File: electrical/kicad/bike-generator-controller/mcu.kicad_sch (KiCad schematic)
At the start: 0 parts

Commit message: feat: integrate controller modules and schematics
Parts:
- added U2: DFR0868 Beetle ESP32-C3, symbol BikeGenerator:DFR0868_Beetle_ESP32-C3
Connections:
- new net +3V3: U2.2 (3V3)
- new net GND: U2.1 (GND_L), U2.10 (GND_R)
- new net I2C_SCL: U2.4 (GPIO1)
- new net I2C_SDA: U2.3 (GPIO0)
- new net INA_ALERT: U2.16 (GPIO2)
- new net POT_CS: U2.7 (GPIO5)
- new net POT_MISO: U2.5 (GPIO4)
- new net POT_MOSI: U2.8 (GPIO7)
- new net POT_SCK: U2.6 (GPIO6)
- new net UART_RX: U2.12 (GPIO20_RX)
- new net UART_TX: U2.13 (GPIO21_TX)
- no-connect marks 0 -> 4
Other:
- note added: "AFFECTATION V1 — GPIO0/1: I²C INA228; GPIO4/5/6/7: SPI DFR0520; GPIO2: ALERT."
- note added: "Alimentation V1 par USB-C. BAT, VIN, GPIO8 et GPIO9 non câblés. Empreinte du module MCU volontairement non affectée avant vérification physique du DFR0868."

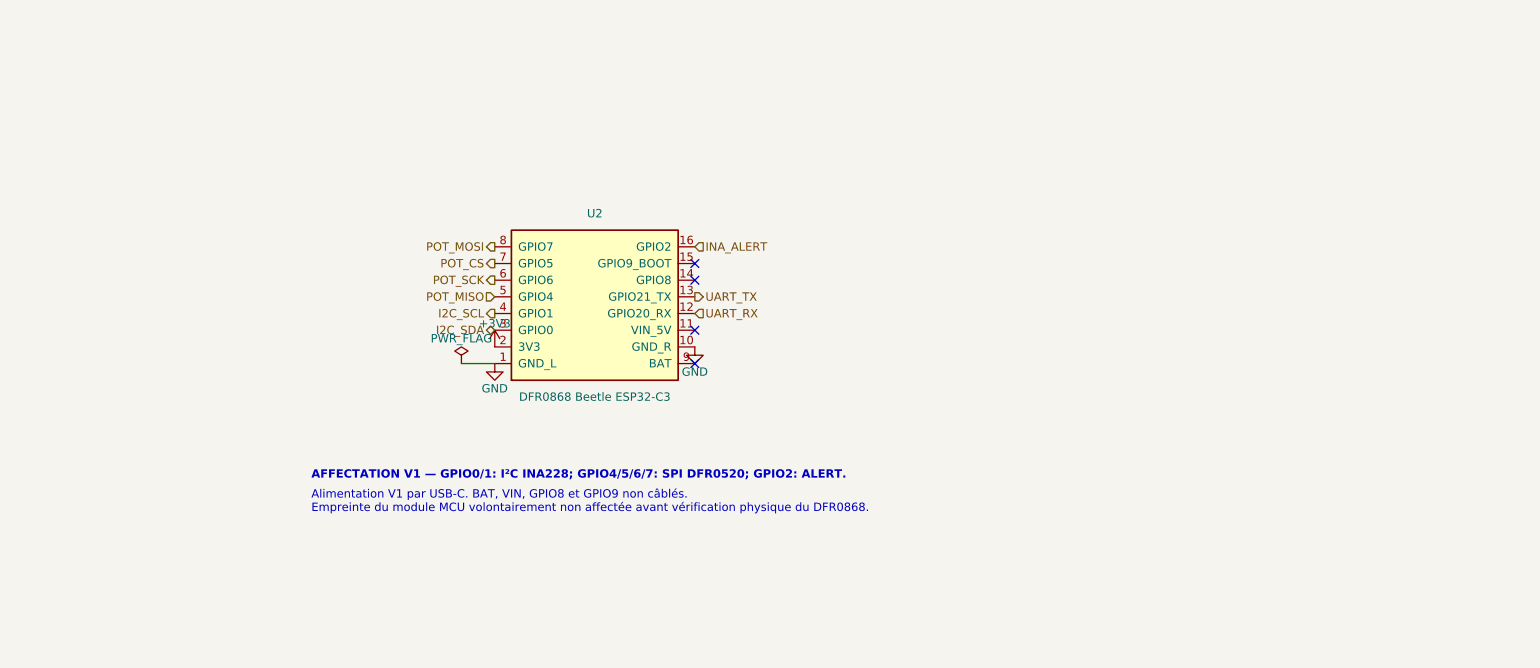
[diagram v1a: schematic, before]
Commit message: feat: add MCU power interlock and battery input
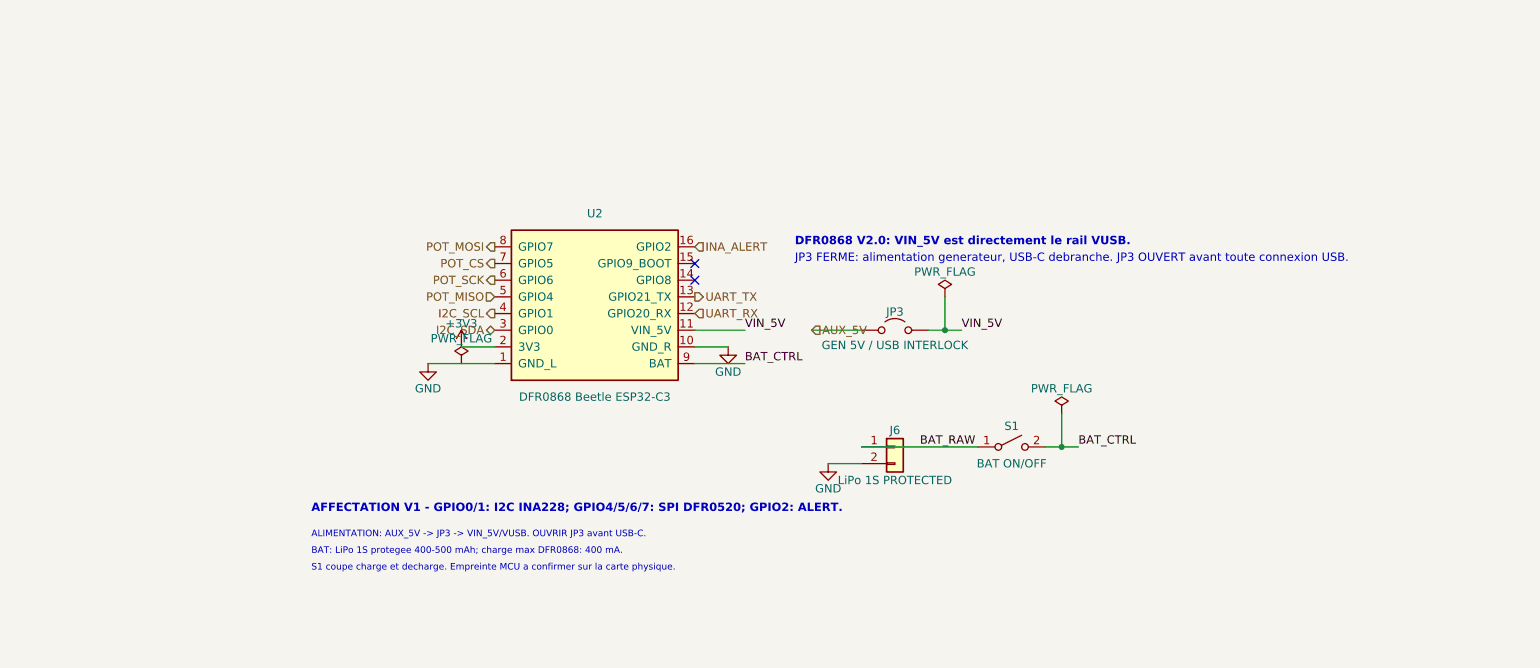
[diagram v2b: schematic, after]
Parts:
- added J6: LiPo 1S PROTECTED, symbol Connector_Generic:Conn_01x02
- added JP3: GEN 5V / USB INTERLOCK, symbol Jumper:Jumper_2_Open
- added S1: BAT ON/OFF, symbol Switch:SW_SPST
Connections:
- net GND: now also J6.2 (Pin_2)
- net VIN_5V: now reaches U2.11 (VIN_5V)
- net VIN_5V: now also JP3.2 (B)
- net BAT_CTRL: now reaches U2.9 (BAT)
- net BAT_CTRL: now also S1.2 (B)
- new net AUX_5V: JP3.1 (A)
- new net BAT_RAW: J6.1 (Pin_1), S1.1 (A)
- no-connect marks 4 -> 2
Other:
- note added: "AFFECTATION V1 - GPIO0/1: I2C INA228; GPIO4/5/6/7: SPI DFR0520; GPIO2: ALERT."
- note added: "ALIMENTATION: AUX_5V -> JP3 -> VIN_5V/VUSB. OUVRIR JP3 avant USB-C."
- note added: "BAT: LiPo 1S protegee 400-500 mAh; charge max DFR0868: 400 mA."
- note added: "DFR0868 V2.0: VIN_5V est directement le rail VUSB."
- note added: "JP3 FERME: alimentation generateur, USB-C debranche. JP3 OUVERT avant toute connexion USB."
- note added: "S1 coupe charge et decharge. Empreinte MCU a confirmer sur la carte physique."
- note removed: "AFFECTATION V1 — GPIO0/1: I²C INA228; GPIO4/5/6/7: SPI DFR0520; GPIO2: ALERT."
- note removed: "Alimentation V1 par USB-C. BAT, VIN, GPIO8 et GPIO9 non câblés. Empreinte du module MCU volontairement non affectée avant vérification physique du DFR0868."

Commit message: feat: add provisional JST battery connection
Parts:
- J6: value LiPo 1S PROTECTED -> LiPo 1S / JST-PH 2.0 / PROV.; footprint (none) -> Connector_JST:JST_PH_S2B-PH-K_1x02_P2.00mm_Horizontal; Status (none) -> PROVISIONAL - verify battery plug pitch and polarity
- JP3: footprint (none) -> Connector_PinHeader_2.54mm:PinHeader_1x02_P2.54mm_Vertical; Status (none) -> PROVISIONAL - removable 2.54 mm shunt
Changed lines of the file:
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@@
 			)
 		)
-		(property "Footprint" ""
+		(property "Footprint" "Connector_PinHeader_2.54mm:PinHeader_1x02_P2.54mm_Vertical"
 			(at 165.1 93.98 0)
 			(hide yes)
@@
 			)
 		)
-	)
+		(property "Status" "PROVISIONAL - removable 2.54 mm shunt"
+			(at 165.1 93.98 0)
+			(hide yes)
+			(effects
+				(font
+					(size 1.27 1.27)
+				)
+			)
+		))
 	(symbol
 		(lib_id "Connector_Generic:Conn_01x02")
@@
 			)
 		)
-		(property "Value" "LiPo 1S PROTECTED"
+		(property "Value" "LiPo 1S / JST-PH 2.0 / PROV."
 			(at 165.1 116.84 0)
 			(effects
@@
 			)
 		)
-		(property "Footprint" ""
+		(property "Footprint" "Connector_JST:JST_PH_S2B-PH-K_1x02_P2.00mm_Horizontal"
 			(at 165.1 111.76 0)
 			(hide yes)
@@
 			)
 		)
-		(property "Datasheet" ""
+		(property "Datasheet" "https://www.jst-mfg.com/product/pdf/eng/ePH.pdf"
 			(at 165.1 111.76 0)
 			(hide yes)
@@
 			)
 		)
-	)
+		(property "Status" "PROVISIONAL - verify battery plug pitch and polarity"
+			(at 165.1 111.76 0)
+			(hide yes)
+			(effects
+				(font
+					(size 1.27 1.27)
+				)
+			)
+		))
 	(symbol
 		(lib_id "Switch:SW_SPST")

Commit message: feat: establish controller PCB V1 design baseline
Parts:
- added TP16, TP17: GND, TestPoint:TestPoint_Pad_D1.5mm, symbol Connector:TestPoint
- S1: value BAT ON/OFF -> 1101M2S3CQE2 / BAT ON-OFF; footprint (none) -> BikeGenerator:SW_1101M2S3CQE2; Contact Rating (none) -> 6 A @ 28 VDC; MPN (none) -> 1101M2S3CQE2; Manufacturer (none) -> C&K / Littelfuse; Physical Pad 3 (none) -> NC - unused throw
- U2: footprint (none) -> BikeGenerator:DFR0868_Beetle_ESP32-C3_V2_Socketed; MPN (none) -> DFR0868; Manufacturer (none) -> DFRobot
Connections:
- net at U2.14 (GPIO8): now also TP17.1
- net at U2.15 (GPIO9_BOOT): now also TP16.1
- net POT_MISO: no longer names the net of U2.5 (GPIO4)
- no-connect marks 2 -> 1
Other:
- moved on the sheet: J6, JP3, S1, U2

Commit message: wip: checkpoint controller routing before review
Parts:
- removed TP16, TP17: GND, TestPoint:TestPoint_Pad_D1.5mm, symbol Connector:TestPoint
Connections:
- net GPIO8_ACTION: now reaches U2.14 (GPIO8)
- net GPIO4_HALL: now reaches U2.5 (GPIO4)
- net UART_RX renamed POT_SHDN
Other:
- moved on the sheet: J6, JP3, S1

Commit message: feat: close controller v1 design and define integrated v2
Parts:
- J6: MPN (none) -> S2B-PH-K-S(LF)(SN); Manufacturer (none) -> JST; Mating Housing (none) -> PHR-2; Safety Note (none) -> VERIFY BATTERY POLARITY BEFORE CONNECTION; NO REVERSE-POLAR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
- U2: Decoupling Review (none) -> Module-level decoupling is integrated on the Beetle ESP32-C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
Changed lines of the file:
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@@
+			)
+		)
+		(property "Manufacturer" "JST"
+			(at 139.7 77.47 0)
+			(hide yes)
+			(show_name no)
+			(do_not_autoplace no)
+			(effects
+				(font
+					(size 1.27 1.27)
+				)
+			)
+		)
+		(property "MPN" "S2B-PH-K-S(LF)(SN)"
+			(at 139.7 77.47 0)
+			(hide yes)
+			(show_name no)
+			(do_not_autoplace no)
+			(effects
+				(font
+					(size 1.27 1.27)
+				)
+			)
+		)
+		(property "Mating Housing" "PHR-2"
+			(at 139.7 77.47 0)
+			(hide yes)
+			(show_name no)
+			(do_not_autoplace no)
+			(effects
+				(font
+					(size 1.27 1.27)
+				)
+			)
+		)
+		(property "Safety Note" "VERIFY BATTERY POLARITY BEFORE CONNECTION; NO REVERSE-POLARITY PROTECTION"
+			(at 139.7 77.47 0)
+			(hide yes)
+			(show_name no)
+			(do_not_autoplace no)
+			(effects
+				(font
+					(size 1.27 1.27)
+				)
 			)
 		)
@@
 			(at 76.2 60.96 0)
 			(hide yes)
+			(show_name no)
+			(do_not_autoplace no)
+			(effects
+				(font
+					(size 1.27 1.27)
+				)
+			)
+		)
+		(property "Decoupling Review" "Module-level decoupling is integrated on the Beetle ESP32-C3 carrier; validate the exact purchased module revision and local capacitor population."
+			(at 76.2 60.96 0)
+			(hide yes)

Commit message: feat: replace v1 battery switch with jumper
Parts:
- JP4: renamed from S1; value 1101M2S3CQE2 / BAT ON-OFF -> BATTERY CONNECT / DISCONNECT; footprint BikeGenerator:SW_1101M2S3CQE2 -> Connector_PinHeader_2.54mm:PinHeader_1x02_P2.54mm_Vertical; symbol Switch:SW_SPST -> Jumper:Jumper_2_Open; Contact Rating 6 A @ 28 VDC -> >= 1 A; MPN 1101M2S3CQE2 -> 1x02 2.54mm header + shorting shunt; Manufacturer C&K / Littelfuse -> Generic; Physical Pad 3 NC - unused throw -> (none)
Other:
- note added: "JP4 OUVERT: batterie isolee (ni charge ni decharge). Empreinte MCU a confirmer sur la carte physique."
- note removed: "S1 coupe charge et decharge. Empreinte MCU a confirmer sur la carte physique."
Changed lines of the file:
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@@
-		)
-	)
-	(text "S1 coupe charge et decharge. Empreinte MCU a confirmer sur la carte physique."
-		(exclude_from_sim no)
-		(at 76.708 143.256 0)
-		(effects
-			(font
-				(size 1 1)
-			)
-			(justify left bottom)
 		)
 	)
@@
 		)
 	)
+  (text "JP4 OUVERT: batterie isolee (ni charge ni decharge). Empreinte MCU a confirmer sur la carte physique."
+    (at 76.708 143.256 0)
+    (effects (font (size 1 1)) (justify left bottom))
+  )
 	(symbol
 		(lib_id "power:GND")
@@
 	)
 	(symbol
-		(lib_id "Switch:SW_SPST")
+		(lib_id "Jumper:Jumper_2_Open")
 		(at 111.76 77.47 180)
 		(unit 1)
@@
 		(in_pos_files yes)
 		(dnp no)
-		(property "Reference" "S1"
+		(property "Reference" "JP4"
 			(at 111.76 80.645 0)
 			(show_name no)
@@
 			)
 		)
-		(property "Value" "1101M2S3CQE2 / BAT ON-OFF"
+		(property "Value" "BATTERY CONNECT / DISCONNECT"
 			(at 111.76 73.914 0)
 			(show_name no)
@@
 			)
 		)
-		(property "Footprint" "BikeGenerator:SW_1101M2S3CQE2"
+		(property "Footprint" "Connector_PinHeader_2.54mm:PinHeader_1x02_P2.54mm_Vertical"
 			(at 111.76 77.47 0)
 			(hide yes)
@@
 			)
 		)
-		(property "Datasheet" "https://www.ckswitches.com/media/1429/1000.pdf"
+		(property "Datasheet" ""
 			(at 111.76 77.47 0)
 			(hide yes)
@@
 			)
 		)
-		(property "Description" "Single Pole Single Throw (SPST) switch"
+		(property "Description" "Removable battery isolation jumper"
 			(at 111.76 77.47 0)
 			(hide yes)
@@
 			)
 		)
-		(property "Contact Rating" "6 A @ 28 VDC"
+		(property "Contact Rating" ">= 1 A"
 			(at 111.76 77.47 0)
 			(hide yes)
@@
 			)
 		)
-		(property "MPN" "1101M2S3CQE2"
+		(property "MPN" "1x02 2.54mm header + shorting shunt"
 			(at 111.76 77.47 0)
 			(hide yes)
@@
 			)
 		)
-		(property "Manufacturer" "C&K / Littelfuse"
+		(property "Manufacturer" "Generic"
 			(at 111.76 77.47 0)
 			(hide yes)
@@
 			)
 		)
-		(property "Physical Pad 3" "NC - unused throw"
+		(property "Physical Pad 3" ""
 			(at 111.76 77.47 0)
 			(hide yes)
@@
 			(project "bike-generator-controller"
 				(path "/3056615a-b94f-4555-a4c5-9bc697b25f9c/3ea255a8-4db3-46df-a7e3-bbbf26e474d6"
-					(reference "S1")
+					(reference "JP4")
 					(unit 1)
 				)
